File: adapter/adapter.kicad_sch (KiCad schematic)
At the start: 13 parts, among them J1 DF3A-2P-2DSA, J10 Ribbon, J11 Ribbon, J12 Ribbon, J9 Ribbon, SW1 CAS-120TA, U1 nice_nano, U2 nice_nano

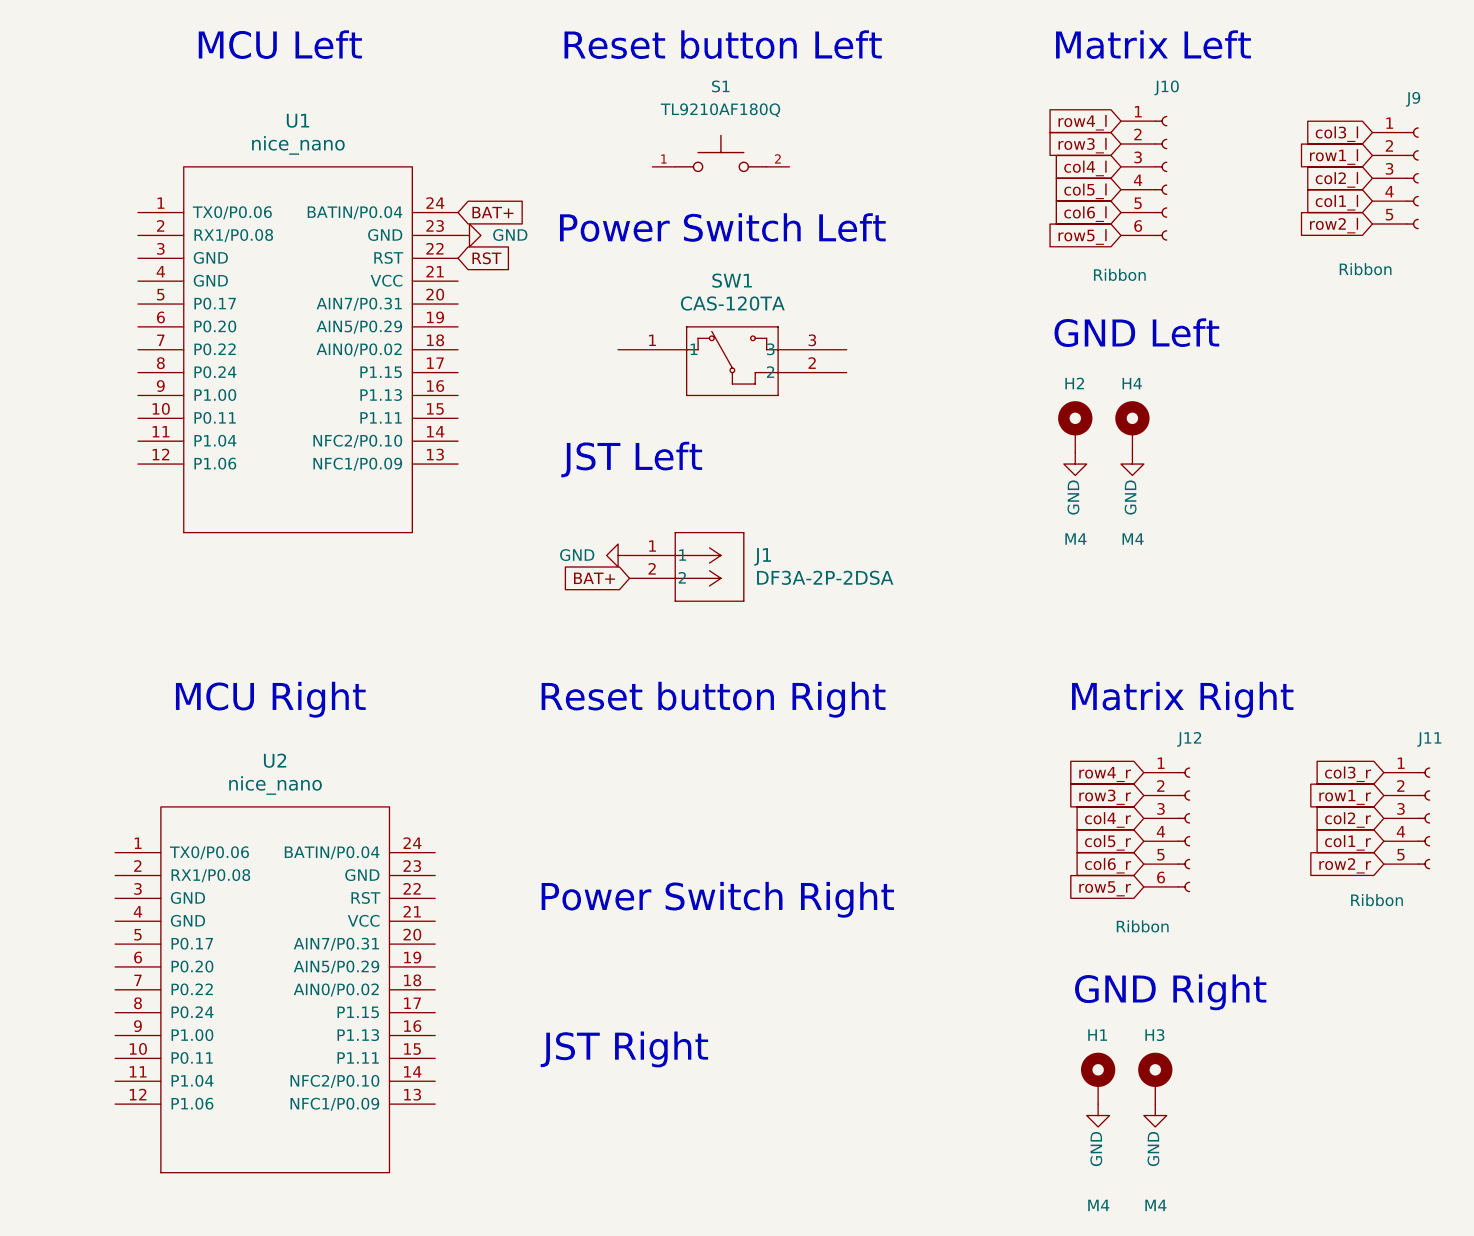
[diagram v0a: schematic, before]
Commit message: Connect all the components in the schematic
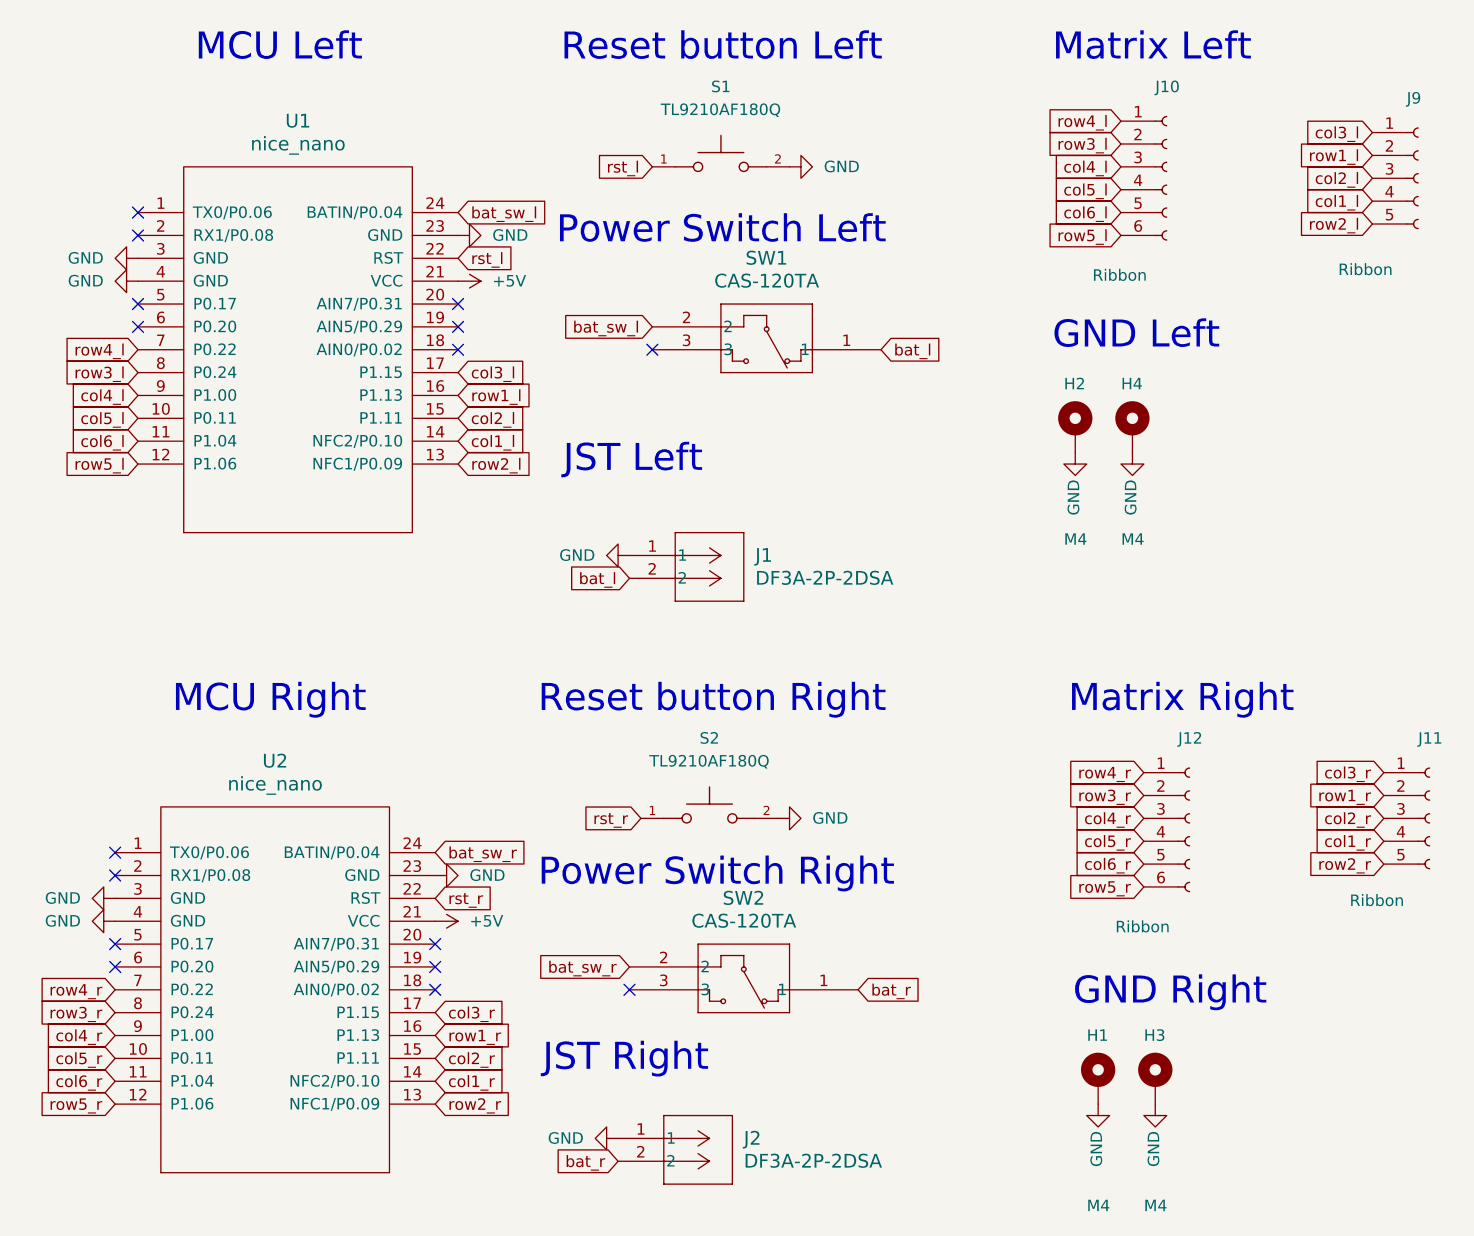
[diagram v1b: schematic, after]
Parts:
- added J2: DF3A-2P-2DSA, CONN_DF3A-2P-2DSA_HIR, symbol DF3A_2P_2DSA:DF3A-2P-2DSA
- added S2: TL9210AF180Q, TL9210AF180Q:SW_TL9210AF180Q, symbol TL9210AF180Q:TL9210AF180Q
- added SW2: CAS-120TA, CAS-120A_NDC, symbol CAS-120TA:CAS-120TA
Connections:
- net RST is gone; now on net rst_l: U1.22 (RST)
- net GND: now also S1.2, U1.3 (GND), U1.4 (GND), U2.23 (GND), U2.3 (GND), U2.4 (GND), J2.1, S2.2
- net col1_l: now also U1.14 (NFC2/P0.10)
- net col1_r: now also U2.14 (NFC2/P0.10)
- net col2_l: now also U1.15 (P1.11)
- net col2_r: now also U2.15 (P1.11)
- net col3_l: now also U1.17 (P1.15)
- net col3_r: now also U2.17 (P1.15)
- net col4_l: now also U1.9 (P1.00)
- net col4_r: now also U2.9 (P1.00)
- net col5_l: now also U1.10 (P0.11)
- net col5_r: now also U2.10 (P0.11)
- net col6_l: now also U1.11 (P1.04)
- net col6_r: now also U2.11 (P1.04)
- net row1_l: now also U1.16 (P1.13)
- net row1_r: now also U2.16 (P1.13)
- net row2_l: now also U1.13 (NFC1/P0.09)
- net row2_r: now also U2.13 (NFC1/P0.09)
- net row3_l: now also U1.8 (P0.24)
- net row3_r: now also U2.8 (P0.24)
- net row4_l: now also U1.7 (P0.22)
- net row4_r: now also U2.7 (P0.22)
- net row5_l: now also U1.12 (P1.06)
- net row5_r: now also U2.12 (P1.06)
- net +5V: now reaches U2.21 (VCC)
- net +5V: now also U1.21 (VCC)
- net rst_r: now reaches U2.22 (RST)
- net rst_r: now also S2.1
- net bat_sw_r: now reaches U2.24 (BATIN/P0.04)
- net bat_sw_r: now also SW2.2
- net bat_l: now reaches SW1.1
- net bat_l: now also J1.2
- net bat_sw_l: now reaches SW1.2
- net bat_sw_l: now also U1.24 (BATIN/P0.04)
- net rst_l: now reaches S1.1
- removed net BAT+: J1.2, U1.24 (BATIN/P0.04)
- new net bat_r: J2.2, SW2.1
- no-connect marks 0 -> 16
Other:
- moved on the sheet: SW1

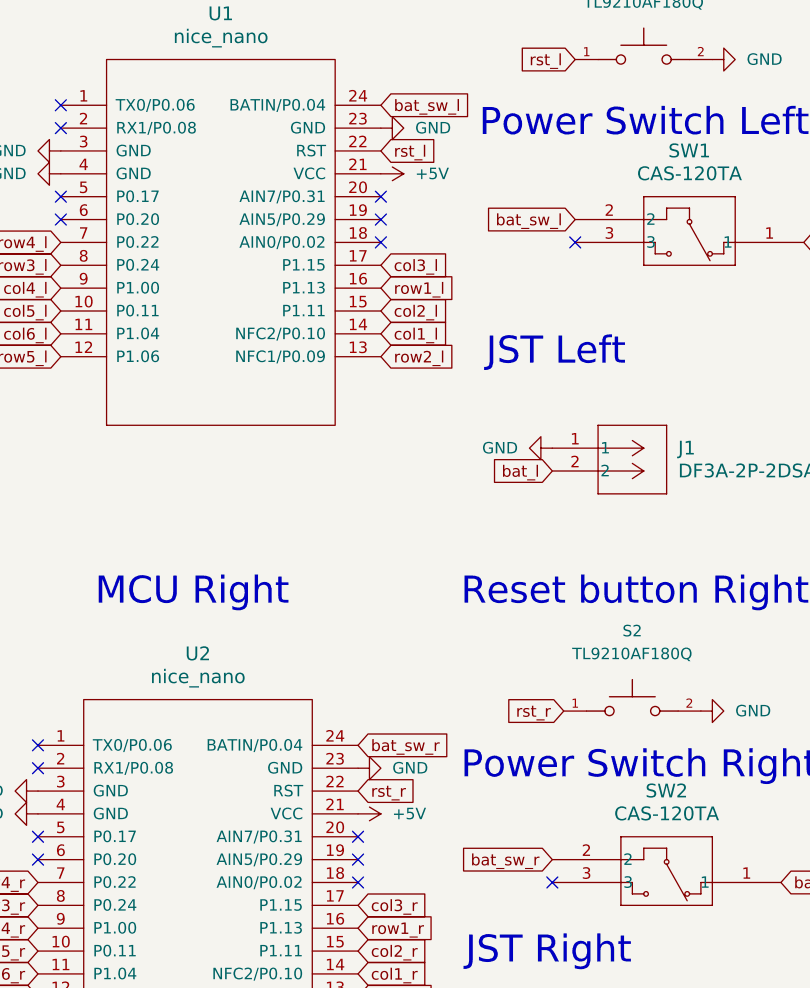
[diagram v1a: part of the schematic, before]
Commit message: Fix all the pcb routes
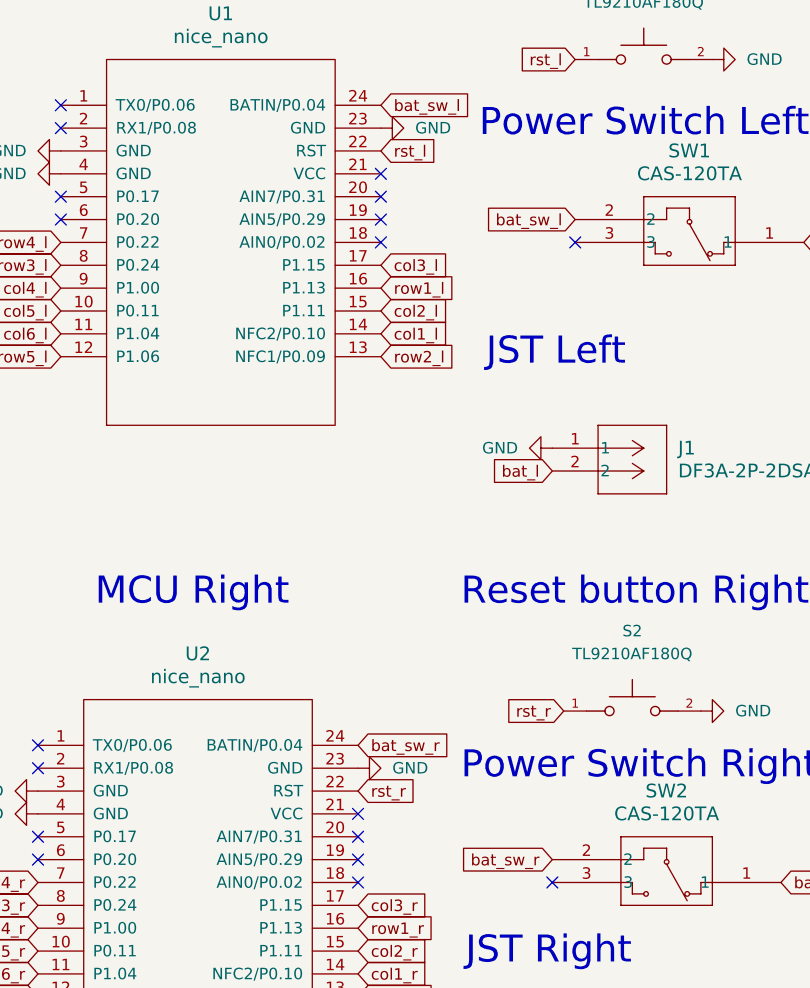
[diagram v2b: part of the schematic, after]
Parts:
- J2: footprint CONN_DF3A-2P-2DSA_HIR -> Library:DF3A_2P_2DSA
- S2: footprint TL9210AF180Q:SW_TL9210AF180Q -> Library:SW_TL9210AF180Q
- SW2: footprint CAS-120A_NDC -> Library:CAS-120A_NDC
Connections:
- net +5V: no longer names the net of U2.21 (VCC)
- net +5V: no longer U1.21 (VCC)
- no-connect marks 16 -> 18
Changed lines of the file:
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@@
 	)
 	(no_connect
+		(at 66.04 52.07)
+	)
+	(no_connect
 		(at 30.48 44.45)
 	)
@@
 	)
 	(no_connect
+		(at 63.5 123.19)
+	)
+	(no_connect
 		(at 27.94 115.57)
 	)
@@
 			)
 		)
-		(property "Footprint" "CAS-120A_NDC"
+		(property "Footprint" "Library:CAS-120A_NDC"
 			(at 110.49 130.81 0)
 			(effects
@@
 	)
 	(symbol
-		(lib_id "power:+5V")
-		(at 63.5 123.19 270)
-		(unit 1)
-		(exclude_from_sim no)
-		(in_bom yes)
-		(on_board yes)
-		(dnp no)
-		(fields_autoplaced yes)
-		(property "Reference" "#PWR012"
-			(at 59.69 123.19 0)
-			(effects
-				(font
-					(size 1.27 1.27)
-				)
-				(hide yes)
-			)
-		)
-		(property "Value" "+5V"
-			(at 67.31 123.1899 90)
-			(effects
-				(font
-					(size 1.27 1.27)
-				)
-				(justify left)
-			)
-		)
-		(property "Footprint" ""
-			(at 63.5 123.19 0)
-			(effects
-				(font
-					(size 1.27 1.27)
-				)
-				(hide yes)
-			)
-		)
-		(property "Datasheet" ""
-			(at 63.5 123.19 0)
-			(effects
-				(font
-					(size 1.27 1.27)
-				)
-				(hide yes)
-			)
-		)
-		(property "Description" "Power symbol creates a global label with name \"+5V\""
-			(at 63.5 123.19 0)
-			(effects
-				(font
-					(size 1.27 1.27)
-				)
-				(hide yes)
-			)
-		)
-		(pin "1"
-		)
-		(instances
-			(project ""
-				(path "/e63e39d7-6ac0-4ffd-8aa3-1841a4541b55"
-					(reference "#PWR012")
-					(unit 1)
-				)
-			)
-		)
-	)
-	(symbol
 		(lib_id "DF3A_2P_2DSA:DF3A-2P-2DSA")
 		(at 83.82 147.32 0)
@@
 			)
 		)
-		(property "Footprint" "CONN_DF3A-2P-2DSA_HIR"
+		(property "Footprint" "Library:DF3A_2P_2DSA"
 			(at 83.82 147.32 0)
 			(effects
@@
 			)
 		)
-		(property "Footprint" "TL9210AF180Q:SW_TL9210AF180Q"
+		(property "Footprint" "Library:SW_TL9210AF180Q"
 			(at 93.98 111.76 0)
 			(effects
@@
 					(unit 1)
 				)
-			)
-		)
-	)
-	(symbol
-		(lib_id "power:+5V")
-		(at 66.04 52.07 270)
-		(unit 1)
-		(exclude_from_sim no)
-		(in_bom yes)
-		(on_board yes)
-		(dnp no)
-		(fields_autoplaced yes)
-		(property "Reference" "#PWR04"
-			(at 62.23 52.07 0)
-			(effects
-				(font
-					(size 1.27 1.27)
-				)
-				(hide yes)
-			)
-		)
-		(property "Value" "+5V"
-			(at 69.85 52.0699 90)
-			(effects
-				(font
-					(size 1.27 1.27)
-				)
-				(justify left)
-			)
-		)
-		(property "Footprint" ""
-			(at 66.04 52.07 0)
-			(effects
-				(font
-					(size 1.27 1.27)
-				)
-				(hide yes)
-			)
-		)
-		(property "Datasheet" ""
-			(at 66.04 52.07 0)
-			(effects
-				(font
-					(size 1.27 1.27)
-				)
-				(hide yes)
-			)
-		)
-		(property "Description" "Power symbol creates a global label with name \"+5V\""
-			(at 66.04 52.07 0)
-			(effects
-				(font
-					(size 1.27 1.27)
-				)
-				(hide yes)
-			)
-		)
-		(pin "1"
-		)
-		(instances
-			(project ""
-				(path "/e63e39d7-6ac0-4ffd-8aa3-1841a4541b55"
-					(reference "#PWR04")
-					(unit 1)
-				)
